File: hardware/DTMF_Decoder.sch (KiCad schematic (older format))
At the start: 36 parts, among them U2 MT8870, U3 MT8870, Y1 3.579545MHZ

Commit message: Update schematic for Issue 2.
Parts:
- added R20, R40: 100K, Resistor_THT:R_Axial_DIN0207_L6.3mm_D2.5mm_P7.62mm_Horizontal, symbol Device:R_US
- R11, R13: value 47K -> 68K
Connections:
- net at R11.2, R7.1, U2.2 (IN-): now also R20.2
- net at U2.3 (GS): now also R20.1
- net at R13.2, R9.1, U3.2 (IN-): now also R40.2
- net at U3.3 (GS): now also R40.1
- net at U3.7 (OSC1): now also C10.2
- net at U3.8 (OSC2): no longer C10.2
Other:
- note added: "2"
- note added: "2020-05-29"
- note removed: "1"
- note removed: "2020-05-17"
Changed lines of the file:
@@
 AR Path="/5EBEBADD/5EC472FB/5EC4FBAE" Ref="R11"  Part="1"
 F 0 "R11" V 4545 2350 50  0000 C CNN
-F 1 "47K" V 4636 2350 50  0000 C CNN
+F 1 "68K" V 4636 2350 50  0000 C CNN
 F 2 "Resistor_THT:R_Axial_DIN0207_L6.3mm_D2.5mm_P7.62mm_Horizontal" V 4790 2340 50  0001 C CNN
 F 3 "~" H 4750 2350 50  0001 C CNN
@@
 	4750 2100 5300 2100
 Wire Wire Line
-	5300 2600 4750 2600
+	5300 2600 5100 2600
 Wire Wire Line
 	4750 2600 4750 2500
@@
 AR Path="/5EBEBADD/5EC472FB/5EC88F42" Ref="R13"  Part="1"
 F 0 "R13" V 4545 5800 50  0000 C CNN
-F 1 "47K" V 4636 5800 50  0000 C CNN
+F 1 "68K" V 4636 5800 50  0000 C CNN
 F 2 "Resistor_THT:R_Axial_DIN0207_L6.3mm_D2.5mm_P7.62mm_Horizontal" V 4790 5790 50  0001 C CNN
 F 3 "~" H 4750 5800 50  0001 C CNN
@@
 	4750 5550 5300 5550
 Wire Wire Line
-	5300 6050 4750 6050
+	5300 6050 5100 6050
 Wire Wire Line
 	4750 6050 4750 5950
@@
 Connection ~ 5050 3050
 Wire Wire Line
-	5050 3600 5050 6500
-Wire Wire Line
-	5050 6500 5300 6500
+	5050 3600 5050 6150
+Wire Wire Line
+	5050 6150 5300 6150
 Wire Wire Line
 	4600 4900 4650 4900
@@
 	0    1    1    0
 $EndComp
-NoConn ~ 5300 6150
 Wire Wire Line
 	6100 2850 7200 2850
@@
 OKI AC125A DTMF Converter - Telco Interface and DTMF Converters
 Text Notes 8150 7650 0    50   ~ 0
-2020-05-17
+2020-05-29
 Text Notes 10550 7650 0    50   ~ 0
-1
+2
 Text Notes 7100 6850 0    100  Italic 20
 OKI AC125A Crossbar PBX DTMF Converter
 Text Notes 7150 7000 0    50   ~ 0
 (c) 2020, Howard M. Harte - WZ2Q
+$Comp
+L Device:R_US R?
+U 1 1 5ED2D7C2
+P 5100 2350
+AR Path="/5ED2D7C2" Ref="R?"  Part="1"
+AR Path="/5EBEBADD/5ED2D7C2" Ref="R?"  Part="1"
+AR Path="/5EBEBADD/5EC472FB/5ED2D7C2" Ref="R20"  Part="1"
+F 0 "R20" V 4895 2350 50  0000 C CNN
+F 1 "100K" V 4986 2350 50  0000 C CNN
+F 2 "Resistor_THT:R_Axial_DIN0207_L6.3mm_D2.5mm_P7.62mm_Horizontal" V 5140 2340 50  0001 C CNN
+F 3 "~" H 5100 2350 50  0001 C CNN
+	1    5100 2350
+	1    0    0    -1
+$EndComp
+Wire Wire Line
+	5100 2500 5100 2600
+Connection ~ 5100 2600
+Wire Wire Line
+	5100 2600 4750 2600
+Wire Wire Line
+	5100 2200 5300 2200
+Wire Wire Line
+	5300 2200 5300 2350
+$Comp
+L Device:R_US R?
+U 1 1 5ED37EDC
+P 5100 5800
+AR Path="/5ED37EDC" Ref="R?"  Part="1"
+AR Path="/5EBEBADD/5ED37EDC" Ref="R?"  Part="1"
+AR Path="/5EBEBADD/5EC472FB/5ED37EDC" Ref="R40"  Part="1"
+F 0 "R40" V 4895 5800 50  0000 C CNN
+F 1 "100K" V 4986 5800 50  0000 C CNN
+F 2 "Resistor_THT:R_Axial_DIN0207_L6.3mm_D2.5mm_P7.62mm_Horizontal" V 5140 5790 50  0001 C CNN
+F 3 "~" H 5100 5800 50  0001 C CNN
+	1    5100 5800
+	1    0    0    -1
+$EndComp
+Wire Wire Line
+	5100 5950 5100 6050
+Wire Wire Line
+	5100 5650 5300 5650
+Wire Wire Line
+	5300 5650 5300 5800
+Connection ~ 5100 6050
+Wire Wire Line
+	5100 6050 4750 6050
+NoConn ~ 5300 6500
 $EndSCHEMATC

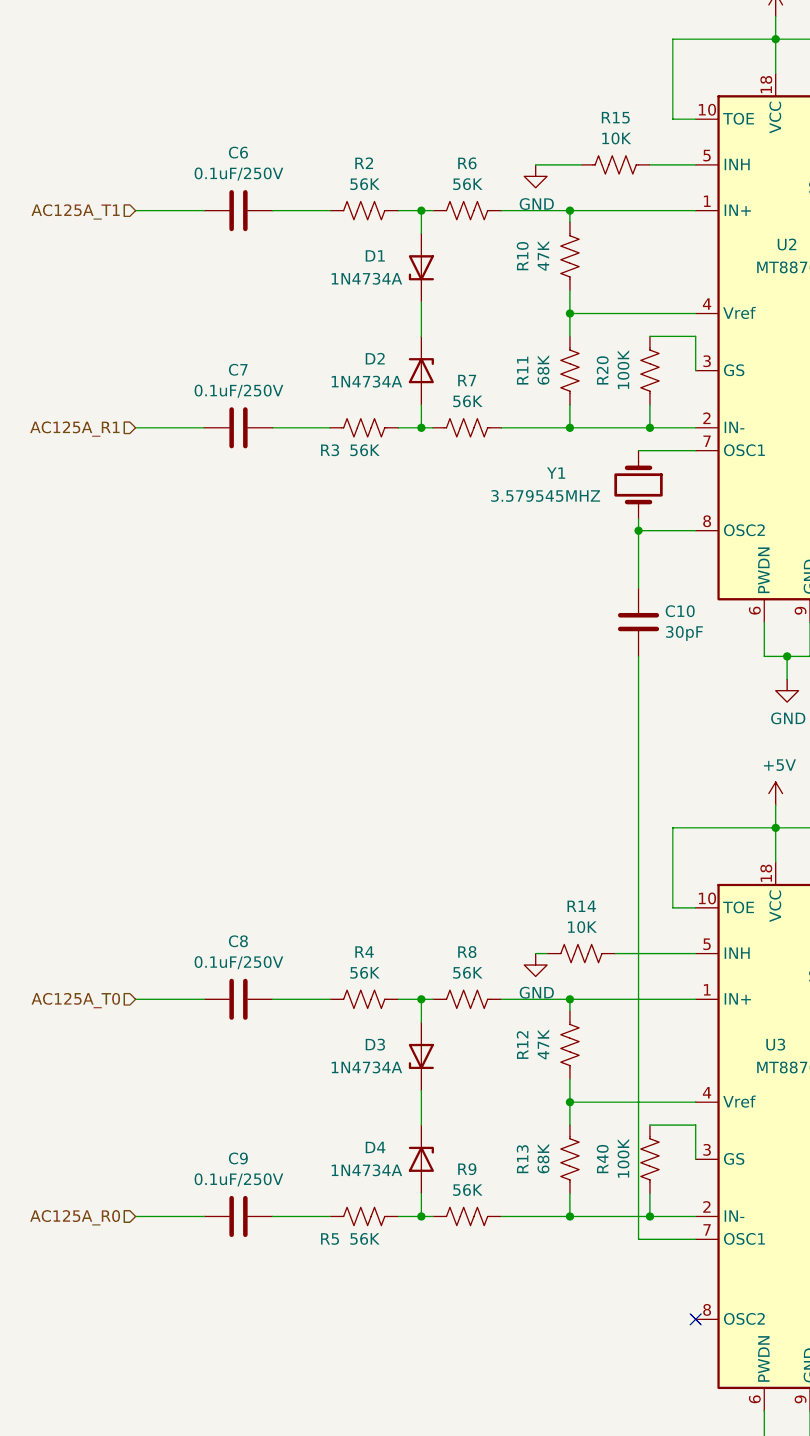
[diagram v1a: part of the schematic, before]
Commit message: Update resistor values for DTMF decoders.
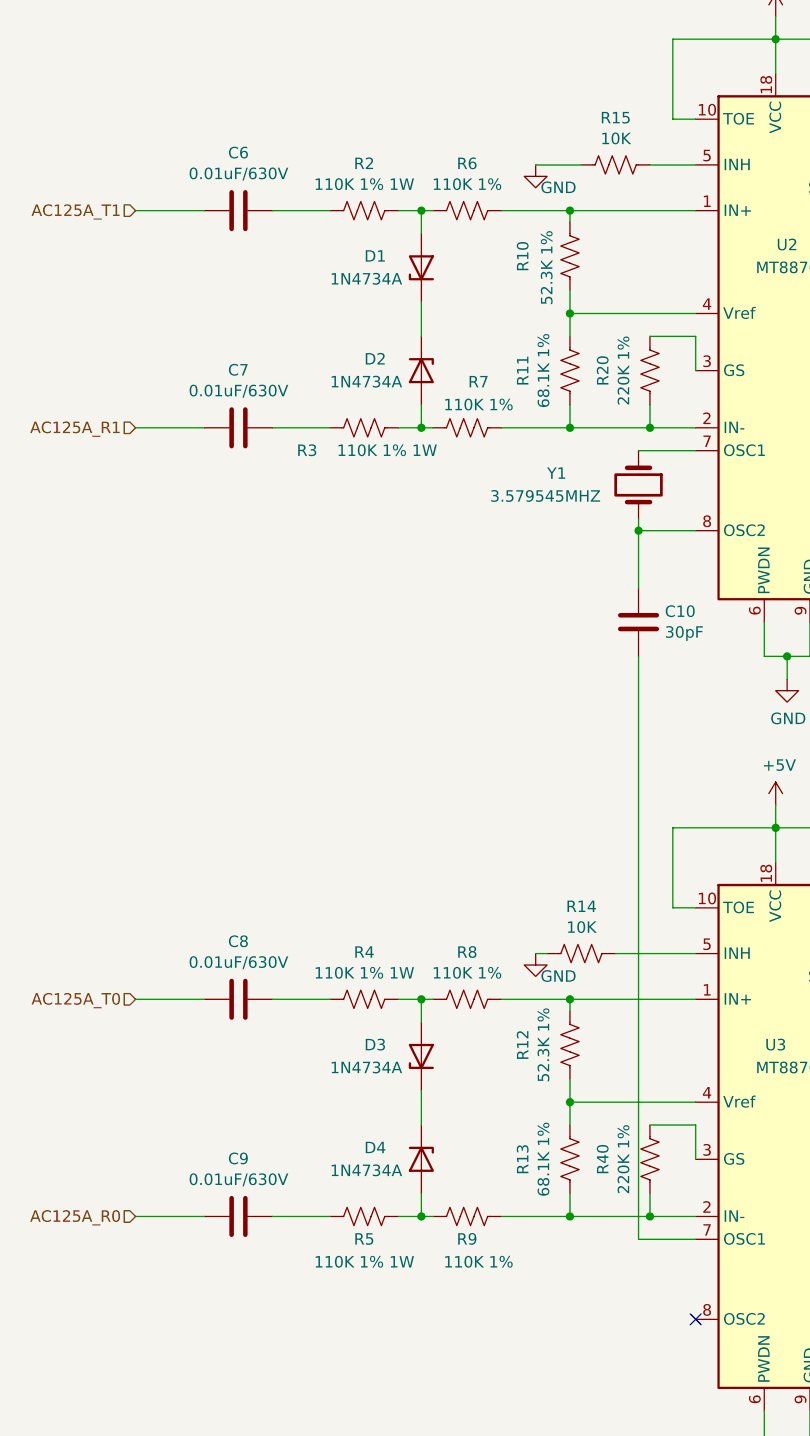
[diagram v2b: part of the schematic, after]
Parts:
- C6, C7, C8, C9: value 0.1uF/250V -> 0.01uF/630V
- R10, R12: value 47K -> 52.3K 1%
- R11, R13: value 68K -> 68.1K 1%
- R2, R3, R4, R5: value 56K -> 110K 1% 1W
- R20, R40: value 100K -> 220K 1%
- R6, R7, R8, R9: value 56K -> 110K 1%
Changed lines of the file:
@@
 P 4600 1450
 F 0 "#PWR014" H 4600 1200 50  0001 C CNN
-F 1 "GND" H 4605 1277 50  0000 C CNN
+F 1 "GND" H 4700 1350 50  0000 C CNN
 F 2 "" H 4600 1450 50  0001 C CNN
 F 3 "" H 4600 1450 50  0001 C CNN
@@
 AR Path="/5EBEBADD/5EC472FB/5EC4E14A" Ref="R10"  Part="1"
 F 0 "R10" V 4545 1850 50  0000 C CNN
-F 1 "47K" V 4636 1850 50  0000 C CNN
+F 1 "52.3K 1%" V 4650 1800 50  0000 C CNN
 F 2 "Resistor_THT:R_Axial_DIN0207_L6.3mm_D2.5mm_P7.62mm_Horizontal" V 4790 1840 50  0001 C CNN
 F 3 "~" H 4750 1850 50  0001 C CNN
@@
 AR Path="/5EBEBADD/5EC472FB/5EC4FBAE" Ref="R11"  Part="1"
 F 0 "R11" V 4545 2350 50  0000 C CNN
-F 1 "68K" V 4636 2350 50  0000 C CNN
+F 1 "68.1K 1%" V 4636 2350 50  0000 C CNN
 F 2 "Resistor_THT:R_Axial_DIN0207_L6.3mm_D2.5mm_P7.62mm_Horizontal" V 4790 2340 50  0001 C CNN
 F 3 "~" H 4750 2350 50  0001 C CNN
@@
 AR Path="/5EBEBADD/5EC472FB/5EC5676E" Ref="R6"  Part="1"
 F 0 "R6" V 4095 1650 50  0000 C CNN
-F 1 "56K" V 4186 1650 50  0000 C CNN
+F 1 "110K 1%" V 4186 1650 50  0000 C CNN
 F 2 "Resistor_THT:R_Axial_DIN0207_L6.3mm_D2.5mm_P7.62mm_Horizontal" V 4340 1640 50  0001 C CNN
 F 3 "~" H 4300 1650 50  0001 C CNN
@@
 AR Path="/5EBEBADD/5EC472FB/5EC57220" Ref="R2"  Part="1"
 F 0 "R2" V 3645 1650 50  0000 C CNN
-F 1 "56K" V 3736 1650 50  0000 C CNN
+F 1 "110K 1% 1W" V 3736 1650 50  0000 C CNN
 F 2 "Resistor_THT:R_Axial_DIN0207_L6.3mm_D2.5mm_P7.62mm_Horizontal" V 3890 1640 50  0001 C CNN
 F 3 "~" H 3850 1650 50  0001 C CNN
@@
 AR Path="/5EBEBADD/5EC5A124" Ref="R?"  Part="1"
 AR Path="/5EBEBADD/5EC472FB/5EC5A124" Ref="R7"  Part="1"
-F 0 "R7" V 4095 2600 50  0000 C CNN
-F 1 "56K" V 4186 2600 50  0000 C CNN
+F 0 "R7" V 4100 2650 50  0000 C CNN
+F 1 "110K 1%" V 4200 2650 50  0000 C CNN
 F 2 "Resistor_THT:R_Axial_DIN0207_L6.3mm_D2.5mm_P7.62mm_Horizontal" V 4340 2590 50  0001 C CNN
 F 3 "~" H 4300 2600 50  0001 C CNN
@@
 AR Path="/5EBEBADD/5EC5A12A" Ref="R?"  Part="1"
 AR Path="/5EBEBADD/5EC472FB/5EC5A12A" Ref="R3"  Part="1"
-F 0 "R3" V 3950 2450 50  0000 C CNN
-F 1 "56K" V 3950 2600 50  0000 C CNN
+F 0 "R3" V 3950 2350 50  0000 C CNN
+F 1 "110K 1% 1W" V 3950 2700 50  0000 C CNN
 F 2 "Resistor_THT:R_Axial_DIN0207_L6.3mm_D2.5mm_P7.62mm_Horizontal" V 3890 2590 50  0001 C CNN
 F 3 "~" H 3850 2600 50  0001 C CNN
@@
 P 3300 1650
 F 0 "C6" V 3048 1650 50  0000 C CNN
-F 1 "0.1uF/250V" V 3139 1650 50  0000 C CNN
+F 1 "0.01uF/630V" V 3139 1650 50  0000 C CNN
 F 2 "Capacitor_THT:C_Disc_D7.5mm_W5.0mm_P5.00mm" H 3338 1500 50  0001 C CNN
 F 3 "~" H 3300 1650 50  0001 C CNN
@@
 P 3300 2600
 F 0 "C7" V 3048 2600 50  0000 C CNN
-F 1 "0.1uF/250V" V 3139 2600 50  0000 C CNN
+F 1 "0.01uF/630V" V 3139 2600 50  0000 C CNN
 F 2 "Capacitor_THT:C_Disc_D7.5mm_W5.0mm_P5.00mm" H 3338 2450 50  0001 C CNN
 F 3 "~" H 3300 2600 50  0001 C CNN
@@
 P 4600 4900
 F 0 "#PWR015" H 4600 4650 50  0001 C CNN
-F 1 "GND" H 4605 4727 50  0000 C CNN
+F 1 "GND" H 4700 4800 50  0000 C CNN
 F 2 "" H 4600 4900 50  0001 C CNN
 F 3 "" H 4600 4900 50  0001 C CNN
@@
 AR Path="/5EBEBADD/5EC472FB/5EC88F3C" Ref="R12"  Part="1"
 F 0 "R12" V 4545 5300 50  0000 C CNN
-F 1 "47K" V 4636 5300 50  0000 C CNN
+F 1 "52.3K 1%" V 4636 5300 50  0000 C CNN
 F 2 "Resistor_THT:R_Axial_DIN0207_L6.3mm_D2.5mm_P7.62mm_Horizontal" V 4790 5290 50  0001 C CNN
 F 3 "~" H 4750 5300 50  0001 C CNN
@@
 AR Path="/5EBEBADD/5EC472FB/5EC88F42" Ref="R13"  Part="1"
 F 0 "R13" V 4545 5800 50  0000 C CNN
-F 1 "68K" V 4636 5800 50  0000 C CNN
+F 1 "68.1K 1%" V 4636 5800 50  0000 C CNN
 F 2 "Resistor_THT:R_Axial_DIN0207_L6.3mm_D2.5mm_P7.62mm_Horizontal" V 4790 5790 50  0001 C CNN
 F 3 "~" H 4750 5800 50  0001 C CNN
@@
 AR Path="/5EBEBADD/5EC472FB/5EC88F52" Ref="R8"  Part="1"
 F 0 "R8" V 4095 5100 50  0000 C CNN
-F 1 "56K" V 4186 5100 50  0000 C CNN
+F 1 "110K 1%" V 4186 5100 50  0000 C CNN
 F 2 "Resistor_THT:R_Axial_DIN0207_L6.3mm_D2.5mm_P7.62mm_Horizontal" V 4340 5090 50  0001 C CNN
 F 3 "~" H 4300 5100 50  0001 C CNN
@@
 AR Path="/5EBEBADD/5EC472FB/5EC88F58" Ref="R4"  Part="1"
 F 0 "R4" V 3645 5100 50  0000 C CNN
-F 1 "56K" V 3736 5100 50  0000 C CNN
+F 1 "110K 1% 1W" V 3736 5100 50  0000 C CNN
 F 2 "Resistor_THT:R_Axial_DIN0207_L6.3mm_D2.5mm_P7.62mm_Horizontal" V 3890 5090 50  0001 C CNN
 F 3 "~" H 3850 5100 50  0001 C CNN
@@
 AR Path="/5EBEBADD/5EC88F5E" Ref="R?"  Part="1"
 AR Path="/5EBEBADD/5EC472FB/5EC88F5E" Ref="R9"  Part="1"
-F 0 "R9" V 4095 6050 50  0000 C CNN
-F 1 "56K" V 4186 6050 50  0000 C CNN
+F 0 "R9" V 4400 6050 50  0000 C CNN
+F 1 "110K 1%" V 4500 6100 50  0000 C CNN
 F 2 "Resistor_THT:R_Axial_DIN0207_L6.3mm_D2.5mm_P7.62mm_Horizontal" V 4340 6040 50  0001 C CNN
 F 3 "~" H 4300 6050 50  0001 C CNN
@@
 AR Path="/5EBEBADD/5EC88F64" Ref="R?"  Part="1"
 AR Path="/5EBEBADD/5EC472FB/5EC88F64" Ref="R5"  Part="1"
-F 0 "R5" V 3950 5900 50  0000 C CNN
-F 1 "56K" V 3950 6050 50  0000 C CNN
+F 0 "R5" V 3950 6050 50  0000 C CNN
+F 1 "110K 1% 1W" V 4050 6050 50  0000 C CNN
 F 2 "Resistor_THT:R_Axial_DIN0207_L6.3mm_D2.5mm_P7.62mm_Horizontal" V 3890 6040 50  0001 C CNN
 F 3 "~" H 3850 6050 50  0001 C CNN
@@
 P 3300 5100
 F 0 "C8" V 3048 5100 50  0000 C CNN
-F 1 "0.1uF/250V" V 3139 5100 50  0000 C CNN
+F 1 "0.01uF/630V" V 3139 5100 50  0000 C CNN
 F 2 "Capacitor_THT:C_Disc_D7.5mm_W5.0mm_P5.00mm" H 3338 4950 50  0001 C CNN
 F 3 "~" H 3300 5100 50  0001 C CNN
@@
 P 3300 6050
 F 0 "C9" V 3048 6050 50  0000 C CNN
-F 1 "0.1uF/250V" V 3139 6050 50  0000 C CNN
+F 1 "0.01uF/630V" V 3139 6050 50  0000 C CNN
 F 2 "Capacitor_THT:C_Disc_D7.5mm_W5.0mm_P5.00mm" H 3338 5900 50  0001 C CNN
 F 3 "~" H 3300 6050 50  0001 C CNN
@@
 AR Path="/5EBEBADD/5EC472FB/5ED2D7C2" Ref="R20"  Part="1"
 F 0 "R20" V 4895 2350 50  0000 C CNN
-F 1 "100K" V 4986 2350 50  0000 C CNN
+F 1 "220K 1%" V 4986 2350 50  0000 C CNN
 F 2 "Resistor_THT:R_Axial_DIN0207_L6.3mm_D2.5mm_P7.62mm_Horizontal" V 5140 2340 50  0001 C CNN
 F 3 "~" H 5100 2350 50  0001 C CNN
@@
 AR Path="/5EBEBADD/5EC472FB/5ED37EDC" Ref="R40"  Part="1"
 F 0 "R40" V 4895 5800 50  0000 C CNN
-F 1 "100K" V 4986 5800 50  0000 C CNN
+F 1 "220K 1%" V 4986 5800 50  0000 C CNN
 F 2 "Resistor_THT:R_Axial_DIN0207_L6.3mm_D2.5mm_P7.62mm_Horizontal" V 5140 5790 50  0001 C CNN
 F 3 "~" H 5100 5800 50  0001 C CNN

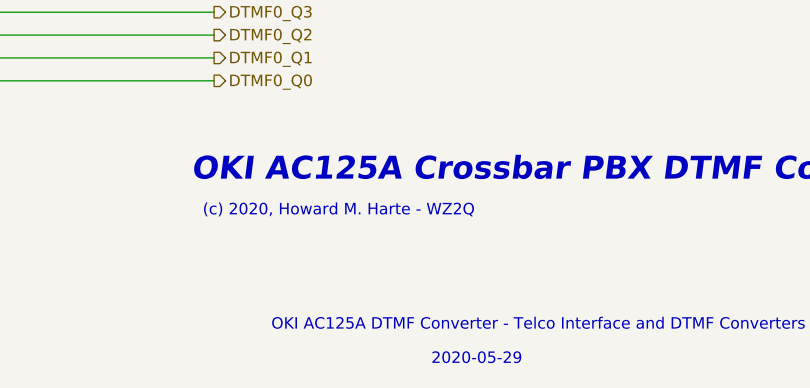
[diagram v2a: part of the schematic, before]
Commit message: Final schematic and PCB layout for Issue 2.
Corrected errors in Issue 1 and fabbed out the PCB.
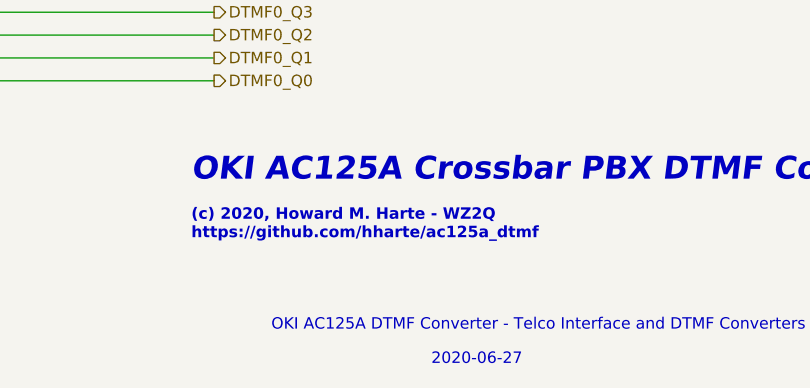
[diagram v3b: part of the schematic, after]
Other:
- note added: "(c) 2020, Howard M. Harte - WZ2Q\nhttps://github.com/hharte/ac125a_dtmf"
- note added: "2020-06-27"
- note removed: "(c) 2020, Howard M. Harte - WZ2Q"
- note removed: "2020-05-29"
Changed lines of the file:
@@
 OKI AC125A DTMF Converter - Telco Interface and DTMF Converters
 Text Notes 8150 7650 0    50   ~ 0
-2020-05-29
+2020-06-27
 Text Notes 10550 7650 0    50   ~ 0
 2
 Text Notes 7100 6850 0    100  Italic 20
 OKI AC125A Crossbar PBX DTMF Converter
-Text Notes 7150 7000 0    50   ~ 0
-(c) 2020, Howard M. Harte - WZ2Q
 $Comp
 L Device:R_US R?
@@
 	5100 6050 4750 6050
 NoConn ~ 5300 6500
+Text Notes 7100 7100 0    50   ~ 10
+(c) 2020, Howard M. Harte - WZ2Q\nhttps://github.com/hharte/ac125a_dtmf
 $EndSCHEMATC
